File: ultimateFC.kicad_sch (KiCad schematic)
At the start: 247 parts, among them J1 Conn_Coaxial, J2 Conn_Coaxial, J3 Conn_Coaxial, J4 Conn_Coaxial, J5 Conn_Coaxial, J6 Conn_Coaxial, J7 USB_B_Micro, SW1 SW_Push, U1 LMR33630CQRNX, U2 TPS62824ADMQ, U3 LMR33620CRNXT, U4 S25FL064L, U5 DPS310, U6 STM32H735VGH6, U7 ICM-20602, U8 BMI270, Y1 CSTNE8M00G550000R0

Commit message: saved schematic
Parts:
- removed TP10, TP11, TP12, TP13, TP14, TP15, TP17, TP19, TP27, TP28, TP39, TP9: Pad, ultimateFC:chonker_TestPoint_Pad_1.5x2.0mm, symbol Connector:TestPoint_Flag
- added D2: White, LED_SMD:LED_0402_1005Metric, symbol Device:LED
- added D3: Red, LED_SMD:LED_0402_1005Metric, symbol Device:LED
- added D4: Yellow, LED_SMD:LED_0402_1005Metric, symbol Device:LED
- added R1: 470R, Resistor_SMD:R_0402_1005Metric, symbol Device:R
- added R2, R5: 100R, Resistor_SMD:R_0402_1005Metric, symbol Device:R
- renumbered D2 to D5, D3 to D6, D4 to D7, D5 to D8, D6 to D9, R7 to R10, R8 to R11, R9 to R12, R10 to R13, R11 to R14, R12 to R15, R13 to R16, R14 to R17, R15 to R18, R16 to R19, R17 to R20, R18 to R21, R19 to R22, R20 to R23, R21 to R24, R22 to R25, R23 to R26, R24 to R27, R25 to R28, R26 to R29, R1 to R3, R27 to R30, R28 to R31, R2 to R4, R3 to R6, R4 to R7, R5 to R8, R6 to R9, TP20 to TP10, TP95 to TP100, TP96 to TP101, TP97 to TP102, TP98 to TP103, TP99 to TP104, TP100 to TP105, TP101 to TP106, TP102 to TP107, TP103 to TP108, TP104 to TP109, TP21 to TP11, TP105 to TP110, TP106 to TP111, TP107 to TP112, TP124 to TP113, TP125 to TP114, TP126 to TP115, TP127 to TP116, TP128 to TP117, TP129 to TP118, TP130 to TP119, TP22 to TP12, TP131 to TP120, TP132 to TP121, TP133 to TP122, TP134 to TP123, TP135 to TP124, TP136 to TP125, TP137 to TP126, TP138 to TP127, TP23 to TP13, TP24 to TP14, TP25 to TP15, TP26 to TP16, TP29 to TP17, TP30 to TP18, TP31 to TP19, TP32 to TP20, TP33 to TP21, TP34 to TP22, TP35 to TP23, TP36 to TP24, TP37 to TP25, TP38 to TP26, TP40 to TP27, TP41 to TP28, TP42 to TP29, TP43 to TP31, TP44 to TP32, TP45 to TP33, TP46 to TP34, TP47 to TP35, TP48 to TP36, TP49 to TP37, TP50 to TP38, TP51 to TP39, TP52 to TP40, TP53 to TP41, TP54 to TP42, TP55 to TP43, TP16 to TP44, TP56 to TP45, TP57 to TP46, TP58 to TP47, TP59 to TP48, TP60 to TP49, TP6 to TP5, TP61 to TP50, TP62 to TP51, TP63 to TP52, TP64 to TP53, TP65 to TP54, TP66 to TP55, TP67 to TP56, TP68 to TP57, TP69 to TP58, TP70 to TP59, TP7 to TP6, TP71 to TP60, TP72 to TP61, TP73 to TP62, TP74 to TP63, TP75 to TP64, TP76 to TP65, TP77 to TP66, TP78 to TP67, TP79 to TP68, TP80 to TP69, TP5 to TP7, TP81 to TP70, TP82 to TP71, TP83 to TP72, TP84 to TP73, TP85 to TP74, TP86 to TP75, TP87 to TP76, TP88 to TP77, TP89 to TP78, TP90 to TP79, TP91 to TP80, TP92 to TP81, TP108 to TP82, TP109 to TP83, TP110 to TP84, TP111 to TP85, TP112 to TP86, TP113 to TP87, TP114 to TP88, TP115 to TP89, TP18 to TP9, TP116 to TP90, TP117 to TP91, TP118 to TP92, TP119 to TP93, TP120 to TP94, TP121 to TP95, TP122 to TP96, TP123 to TP97, TP93 to TP98, TP94 to TP99
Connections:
- net +10V: now also R1.1
- net +3V3: now also R5.1
- net +5V: now also R2.1
- net GND: now also U2.2 (PG), D2.1 (K), D3.1 (K), D4.1 (K)
- new net: D4.2 (A), R5.2
- new net: D2.2 (A), R1.2
- new net: D3.2 (A), R2.2
- no-connect marks 10 -> 9

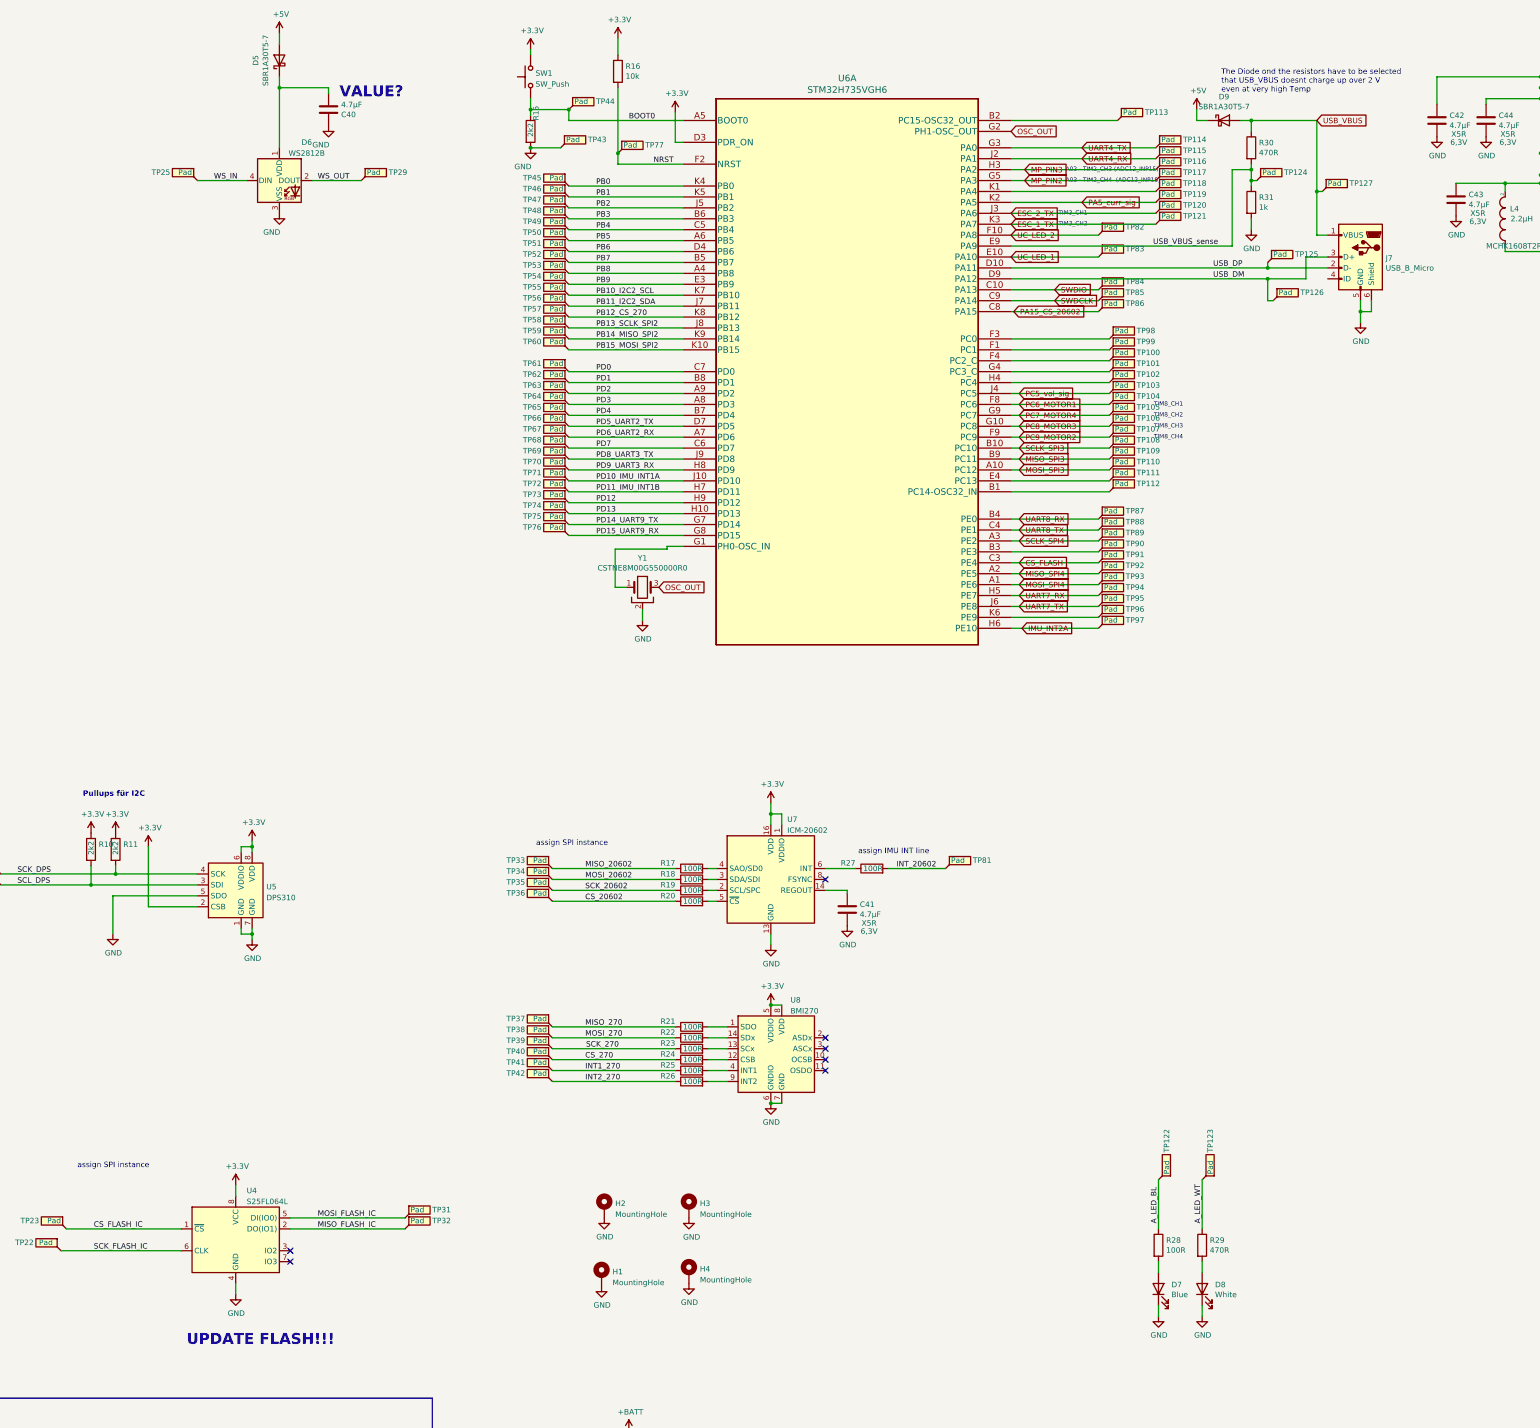
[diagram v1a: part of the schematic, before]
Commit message: pad labeling and silkscreen
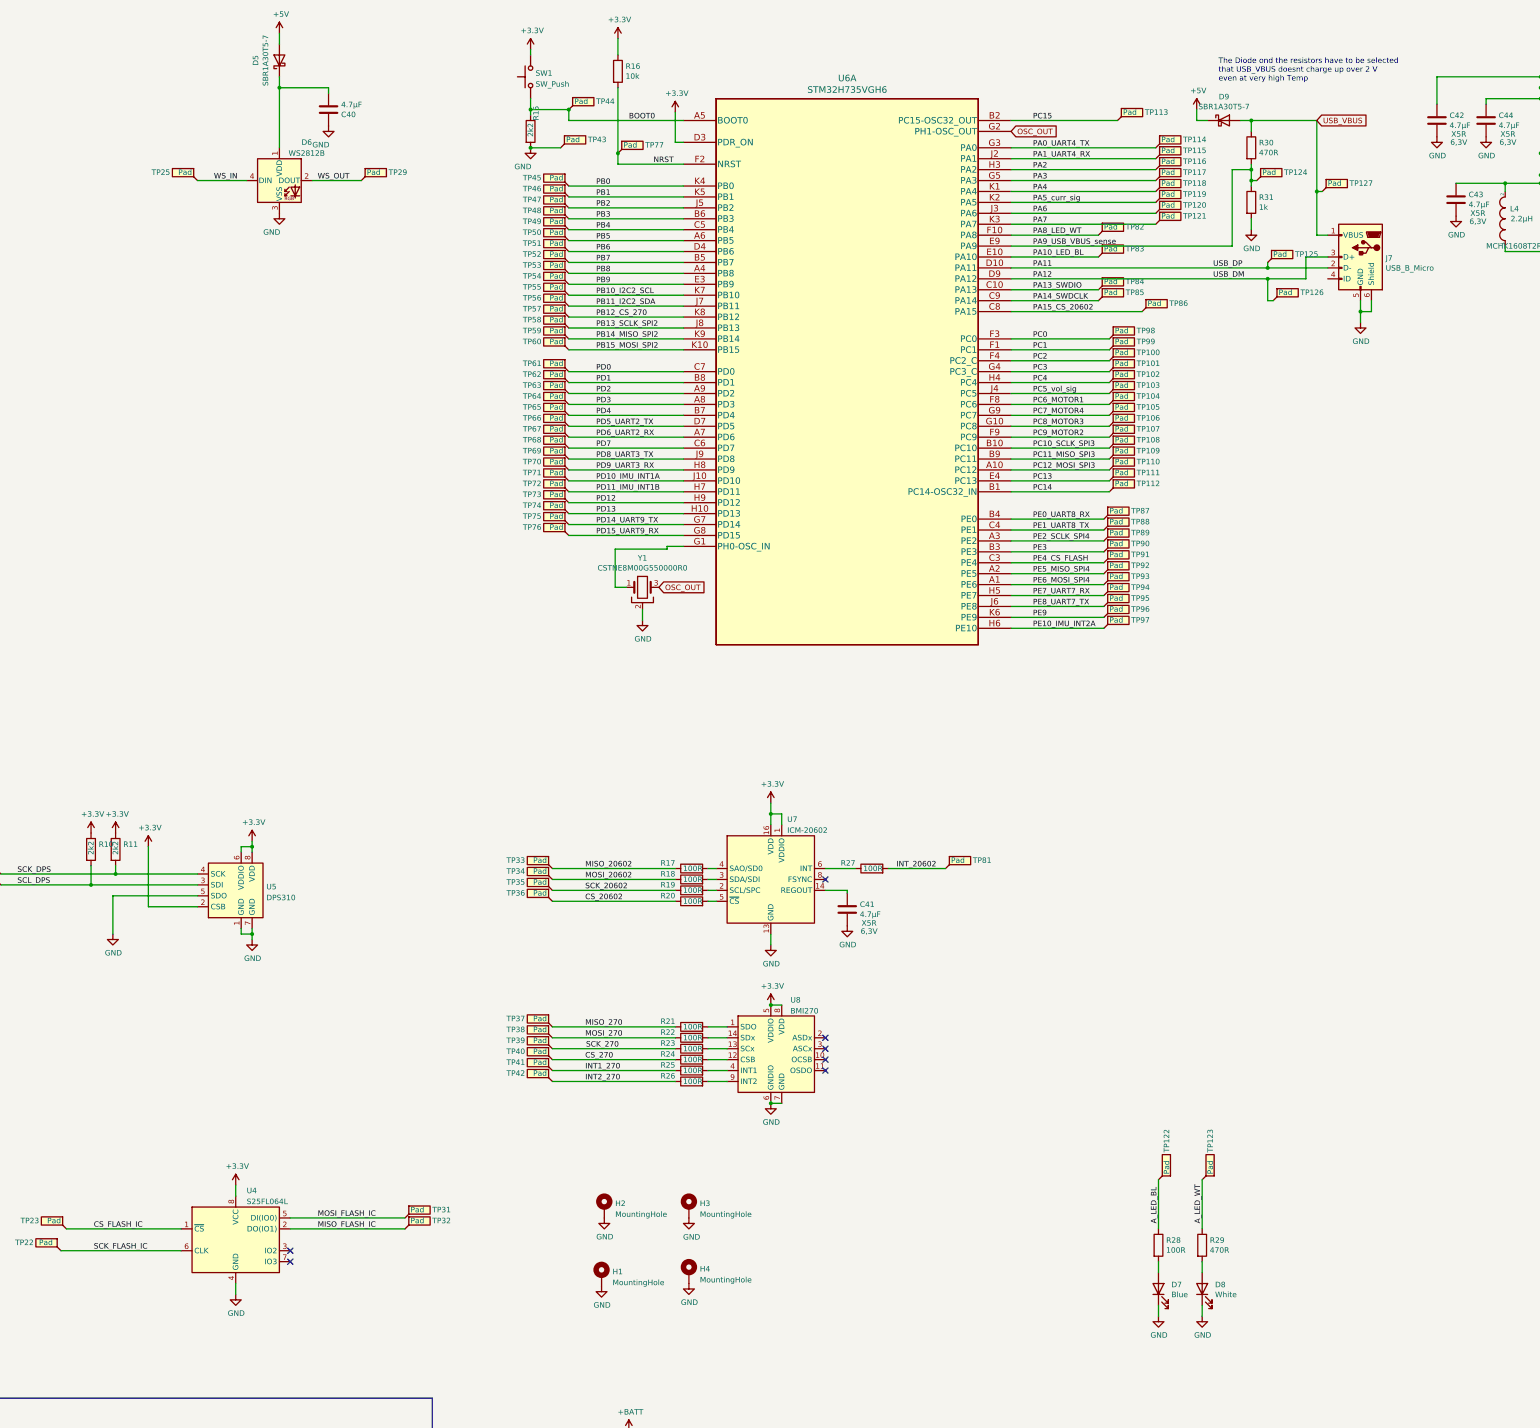
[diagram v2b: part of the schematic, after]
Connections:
- net PC14: now reaches TP112.1, U6.B1 (PC14-OSC32_IN)
- net PC15: now reaches TP113.1, U6.B2 (PC15-OSC32_OUT)
- net PE3: now reaches TP90.1, U6.B3 (PE3)
- net PC13: now reaches TP111.1, U6.E4 (PC13)
- net PC1: now reaches TP99.1, U6.F1 (PC1)
- net PC0: now reaches TP98.1, U6.F3 (PC0)
- net PC2: now reaches TP100.1, U6.F4 (PC2_C)
- net PC3: now reaches TP101.1, U6.G4 (PC3_C)
- net PC4: now reaches TP102.1, U6.H4 (PC4)
- net PA4: now reaches TP118.1, U6.K1 (PA4)
- net PE9: now reaches TP96.1, U6.K6 (PE9)
- net CS_FLASH renamed PE4_CS_FLASH
- net ESC_1_TX renamed PA7
- net ESC_2_TX renamed PA6
- net IMU_INT2A renamed PE10_IMU_INT2A
- net MISO_SPI3 renamed PC11_MISO_SPI3
- net MISO_SPI4 renamed PE5_MISO_SPI4
- net MOSI_SPI3 renamed PC12_MOSI_SPI3
- net MOSI_SPI4 renamed PE6_MOSI_SPI4
- net MP_PIN2 renamed PA3
- net MP_PIN3 renamed PA2
- net SCLK_SPI3 renamed PC10_SCLK_SPI3
- net SCLK_SPI4 renamed PE2_SCLK_SPI4
- net SWDCLK renamed PA14_SWDCLK
- net SWDIO renamed PA13_SWDIO
- net UART4_RX renamed PA1_UART4_RX
- net UART4_TX renamed PA0_UART4_TX
- net UART7_RX renamed PE7_UART7_RX
- net UART7_TX renamed PE8_UART7_TX
- net UART8_RX renamed PE0_UART8_RX
- net UART8_TX renamed PE1_UART8_TX
- net UC_LED_1 renamed PA10_LED_BL
- net UC_LED_2 renamed PA8_LED_WT
- net USB_DM renamed PA12
- net USB_DP renamed PA11
- net USB_VBUS_sense renamed PA9_USB_VBUS_sense
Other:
- note removed: "A02 - TIM2_CH3 (ADC12_INP15)"
- note removed: "A03 - TIM2_CH4 (ADC12_INP18)"
- note removed: "Pullups für I2C"
- note removed: "TIM3_CH1"
- note removed: "TIM3_CH2"
- note removed: "TIM8_CH1"
- note removed: "TIM8_CH2"
- note removed: "TIM8_CH3"
- note removed: "TIM8_CH4"
- note removed: "UPDATE FLASH!!!"
- note removed: "VALUE?"
- note removed: "assign IMU INT line"
- note removed: "assign SPI instance"
- moved on the sheet: TP86, TP87, TP88, TP89, TP90, TP91, TP92, TP93, TP94, TP95, TP96, TP97

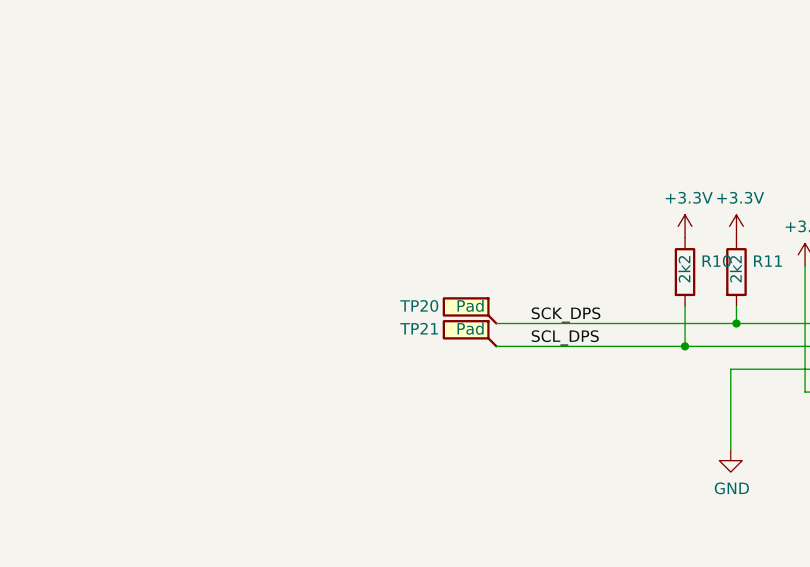
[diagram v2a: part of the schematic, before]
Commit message: add labeling error note in schematic
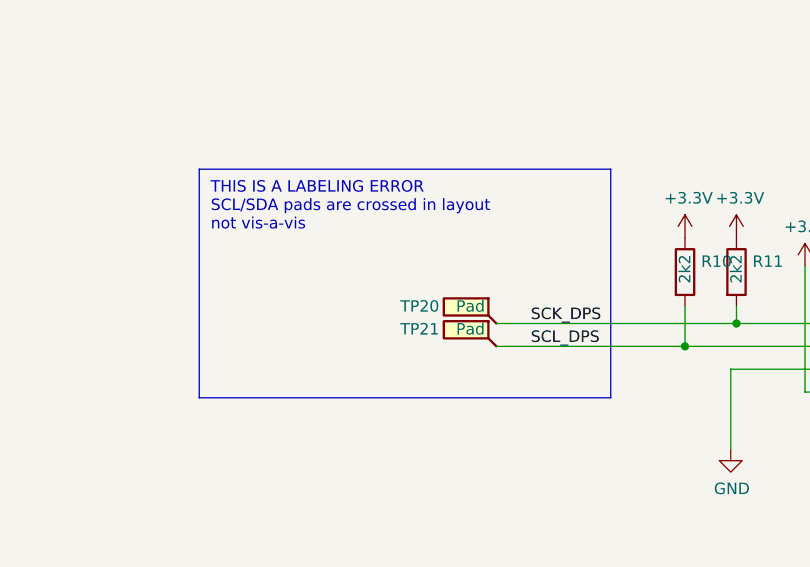
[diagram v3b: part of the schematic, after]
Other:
- note added: "THIS IS A LABELING ERROR SCL/SDA pads are crossed in layout not vis-a-vis"
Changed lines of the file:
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@@
+    (stroke (width 0) (type default) (color 0 0 0 0))
+  )
+  (polyline (pts (xy 396.24 226.695) (xy 350.52 226.695))
     (stroke (width 0) (type default) (color 0 0 0 0))
   )
@@
     (stroke (width 0) (type default) (color 0 0 0 0))
   )
+  (polyline (pts (xy 396.24 201.295) (xy 396.24 226.695))
+    (stroke (width 0) (type default) (color 0 0 0 0))
+  )
   (wire (pts (xy 661.67 40.64) (xy 661.67 43.18))
     (stroke (width 0) (type default) (color 0 0 0 0))
@@
     (stroke (width 0) (type default) (color 0 0 0 0))
   )
+  (polyline (pts (xy 350.52 201.295) (xy 350.52 226.695))
+    (stroke (width 0) (type default) (color 0 0 0 0))
+  )
   (wire (pts (xy 222.25 379.73) (xy 222.885 379.73))
     (stroke (width 0) (type default) (color 0 0 0 0))
@@
   )
   (wire (pts (xy 689.61 59.69) (xy 690.88 59.69))
+    (stroke (width 0) (type default) (color 0 0 0 0))
+  )
+  (polyline (pts (xy 350.52 201.295) (xy 396.24 201.295))
     (stroke (width 0) (type default) (color 0 0 0 0))
   )
@@
     (effects (font (size 1.27 1.27)) (justify left bottom))
   )
+  (text "THIS IS A LABELING ERROR\nSCL/SDA pads are crossed in layout\nnot vis-a-vis"
+    (at 351.79 208.28 0)
+    (effects (font (size 1.27 1.27)) (justify left bottom))
+  )

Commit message: schematic: add vis-a-vis pad notes
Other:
- note added: "next to I2C2 pads in layout"
- note added: "next to PA10 pad in layout"
- note added: "next to PA8 pad in layout"
- note added: "next to PB12"
- note added: "next to PB12 and PA15"
- note added: "next to PC5 pad in layout"
- note added: "next to PD10"
- note added: "next to PD10 or PD11"
- note added: "next to PD2 pad in layout"
- note added: "next to PE10"
- note added: "next to SPI2 pads in layout"
- note added: "next to SPI3 and SPI2 pads in layout"
- note added: "next to SPI4 (CS: PE4) pads in layout"
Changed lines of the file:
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@@
   (text "THIS IS A LABELING ERROR\nSCL/SDA pads are crossed in layout\nnot vis-a-vis"
     (at 351.79 208.28 0)
+    (effects (font (size 1.27 1.27) (thickness 0.254) bold) (justify left bottom))
+  )
+  (text "next to SPI3 and SPI2\npads in layout" (at 497.84 220.98 180)
+    (effects (font (size 1.27 1.27)) (justify right bottom))
+  )
+  (text "TFM252012ALMA1R0MTAA as alternative" (at 372.11 353.695 0)
     (effects (font (size 1.27 1.27)) (justify left bottom))
   )
-  (text "TFM252012ALMA1R0MTAA as alternative" (at 372.11 353.695 0)
+  (text "next to PA8 pad in layout" (at 666.115 276.86 90)
+    (effects (font (size 1.27 1.27)) (justify left bottom))
+  )
+  (text "next to PD10" (at 497.84 263.525 180)
+    (effects (font (size 1.27 1.27)) (justify right bottom))
+  )
+  (text "next to PD2 pad in layout" (at 414.655 56.515 180)
+    (effects (font (size 1.27 1.27)) (justify right bottom))
+  )
+  (text "next to PD10 or PD11" (at 614.68 215.9 0)
     (effects (font (size 1.27 1.27)) (justify left bottom))
   )
@@
   )
   (text "Buck for 3,3V" (at 160.02 343.535 0)
+    (effects (font (size 1.27 1.27)) (justify left bottom))
+  )
+  (text "next to I2C2 pads\nin layout" (at 353.695 219.075 0)
+    (effects (font (size 1.27 1.27)) (justify left bottom))
+  )
+  (text "next to PA10 pad in layout" (at 655.955 276.86 90)
+    (effects (font (size 1.27 1.27)) (justify left bottom))
+  )
+  (text "next to SPI4 (CS: PE4)\npads in layout" (at 459.105 308.61 0)
     (effects (font (size 1.27 1.27)) (justify left bottom))
   )
@@
     (effects (font (size 1.27 1.27)) (justify left bottom))
   )
+  (text "next to PE10" (at 497.84 266.065 180)
+    (effects (font (size 1.27 1.27)) (justify right bottom))
+  )
   (text "3300mV (ref) / (1k/(1k+10k))\n=36,3 Fullscale" (at 278.765 292.735 0)
     (effects (font (size 1.27 1.27)) (justify left bottom))
@@
   (text "Current and voltage measurement" (at 266.7 276.86 0)
     (effects (font (size 1.27 1.27)) (justify left bottom))
+  )
+  (text "next to PB12 and PA15" (at 497.84 223.52 180)
+    (effects (font (size 1.27 1.27)) (justify right bottom))
+  )
+  (text "next to PB12" (at 497.84 260.985 180)
+    (effects (font (size 1.27 1.27)) (justify right bottom))
   )
   (text "fc=1,6kHz" (at 276.86 327.66 0)
@@
     (effects (font (size 1.27 1.27)) (justify left bottom))
   )
+  (text "next to PC5 pad in layout" (at 297.18 304.165 0)
+    (effects (font (size 1.27 1.27)) (justify left bottom))
+  )
   (text "PMEG1030EJ,115 lower dropout\nalternative for 3A" (at 315.595 357.505 0)
     (effects (font (size 1.27 1.27)) (justify left bottom))
   )
+  (text "next to SPI2\npads in layout" (at 497.84 257.81 180)
+    (effects (font (size 1.27 1.27)) (justify right bottom))
+  )
   (label "PC4" (at 623.57 104.14 0)

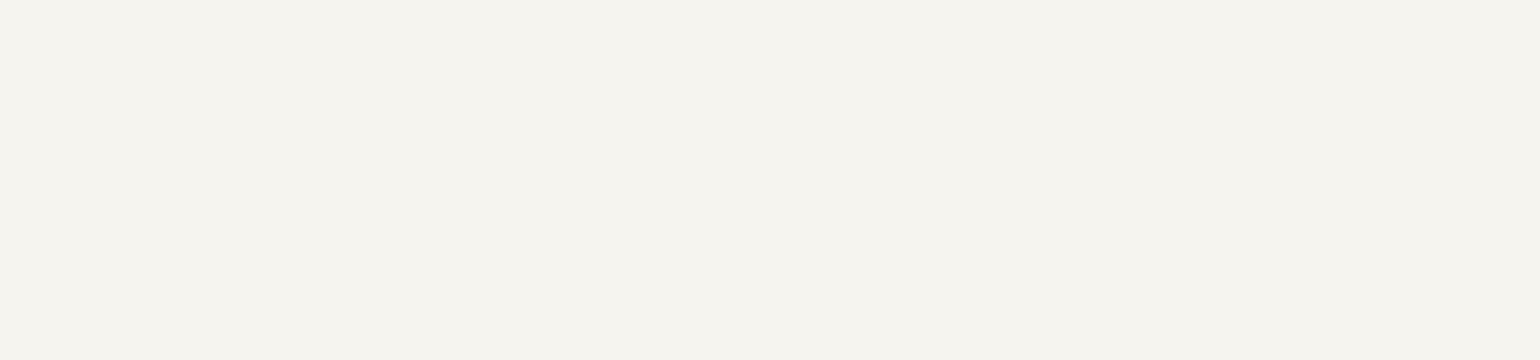
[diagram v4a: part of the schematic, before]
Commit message: add license
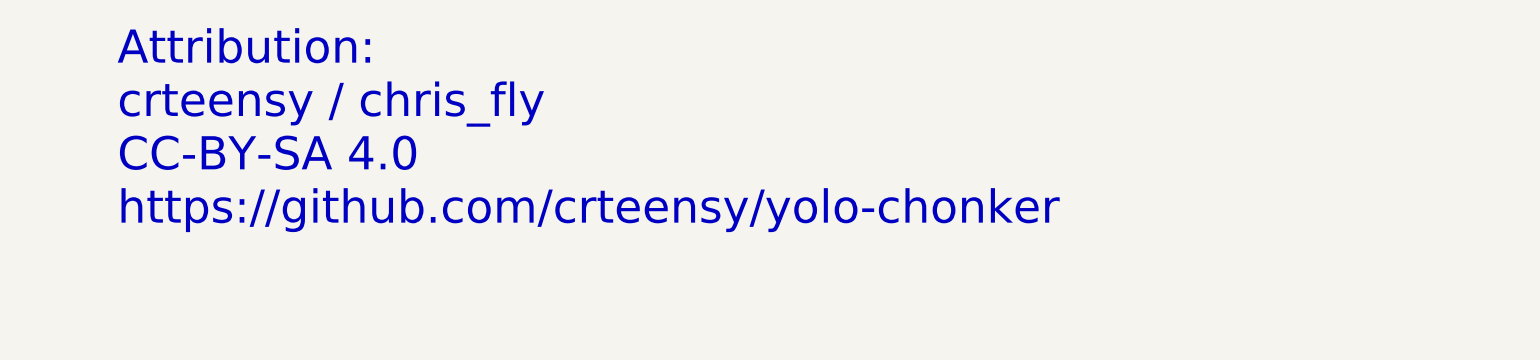
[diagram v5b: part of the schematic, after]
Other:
- note added: "Attribution: crteensy / chris_fly CC-BY-SA 4.0 https://github.com/crteensy/yolo-chonker"
- title: Yolo FC -> Yolo Chonker dev FC
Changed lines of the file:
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@@
   (paper "User" 799.998 419.989)
   (title_block
-    (title "Yolo FC")
-    (date "2021-04-24")
-    (rev "1")
+    (title "Yolo Chonker dev FC")
+    (date "2023-03-03")
+    (rev "0.1")
   )
   (junction (at 175.26 257.81) (diameter 0) (color 0 0 0 0)
@@
     (effects (font (size 1.27 1.27)) (justify left bottom))
   )
+  (text "Attribution:\ncrteensy / chris_fly\nCC-BY-SA 4.0\nhttps://github.com/crteensy/yolo-chonker"
+    (at 36.83 49.53 0)
+    (effects (font (size 5.08 5.08)) (justify left bottom))
+  )
   (text "Current and voltage measurement" (at 266.7 276.86 0)

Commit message: update as-built state schematic annotations low temp layer in layout
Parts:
- R1: value 470R -> 4k7
- R2: value 100R -> 1k5
- R28: value 100R -> 560R
- R29: value 470R -> 560R
- R5: value 100R -> 680R
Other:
- note added: "4x low temp paste"
- note added: "6x low temp paste"
- note added: "low temp paste"
- note added: "power system integrity measurement coax connectors"
- note added: "solder bridge: leave open for 5V out close for 10V out"
- note removed: "excluded from board"
- moved on the sheet: D2, D3, D4, R1, R2, R5, TP1, TP10, TP11, TP12, TP13, TP14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

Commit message: fix errors and mistakes, update schematic
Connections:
- net SCK_DPS is gone; now on net SCL_DPS: R11.2, TP20.1, U5.4 (SCK)
- net SCL_DPS: no longer R10.2, TP21.1, U5.3 (SDI)
- new net SDA_DPS: R10.2, TP21.1, U5.3 (SDI)
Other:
- note removed: "THIS IS A LABELING ERROR SCL/SDA pads are crossed in layout not vis-a-vis"

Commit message: minor layout tweaks
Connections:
- net PA11 renamed PA11_USB_DM
- net PA12 renamed PA12_USB_DP
